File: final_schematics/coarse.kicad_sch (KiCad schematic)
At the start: 7 parts, among them J3 RJ9, SW1 SW_SPST, SW2 SW_SPST, SW3 SW_SPST, SW4 SW_SPST, SW5 SW_SPST

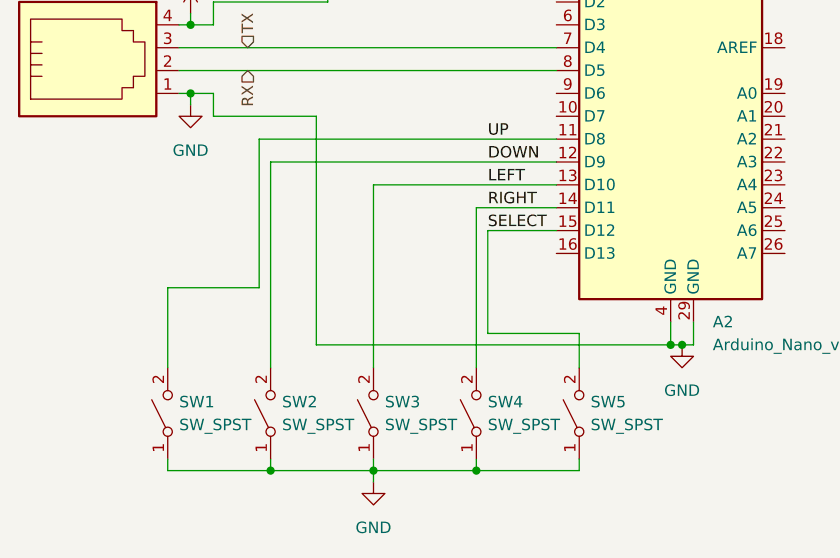
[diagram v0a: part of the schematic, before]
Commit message: Test code on main board
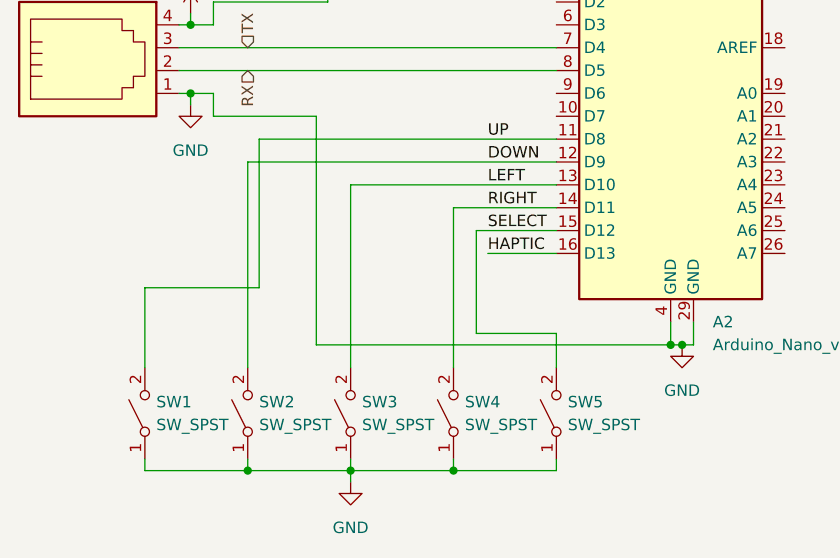
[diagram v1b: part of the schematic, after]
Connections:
- net HAPTIC: now reaches A2.16 (D13)
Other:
- moved on the sheet: SW1, SW2, SW3, SW4, SW5

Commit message: Almost ready to play a full game
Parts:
- added M2: Motor_DC, symbol Motor:Motor_DC
- added Q2: NPN, symbol Simulation_SPICE:NPN
- added R2: 330, symbol Device:R
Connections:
- net +5V: now also M2.1 (+)
- net GND: now also Q2.3 (E)
- net HAPTIC: now also R2.1
- new net: M2.2 (-), Q2.1 (C)
- new net: Q2.2 (B), R2.2

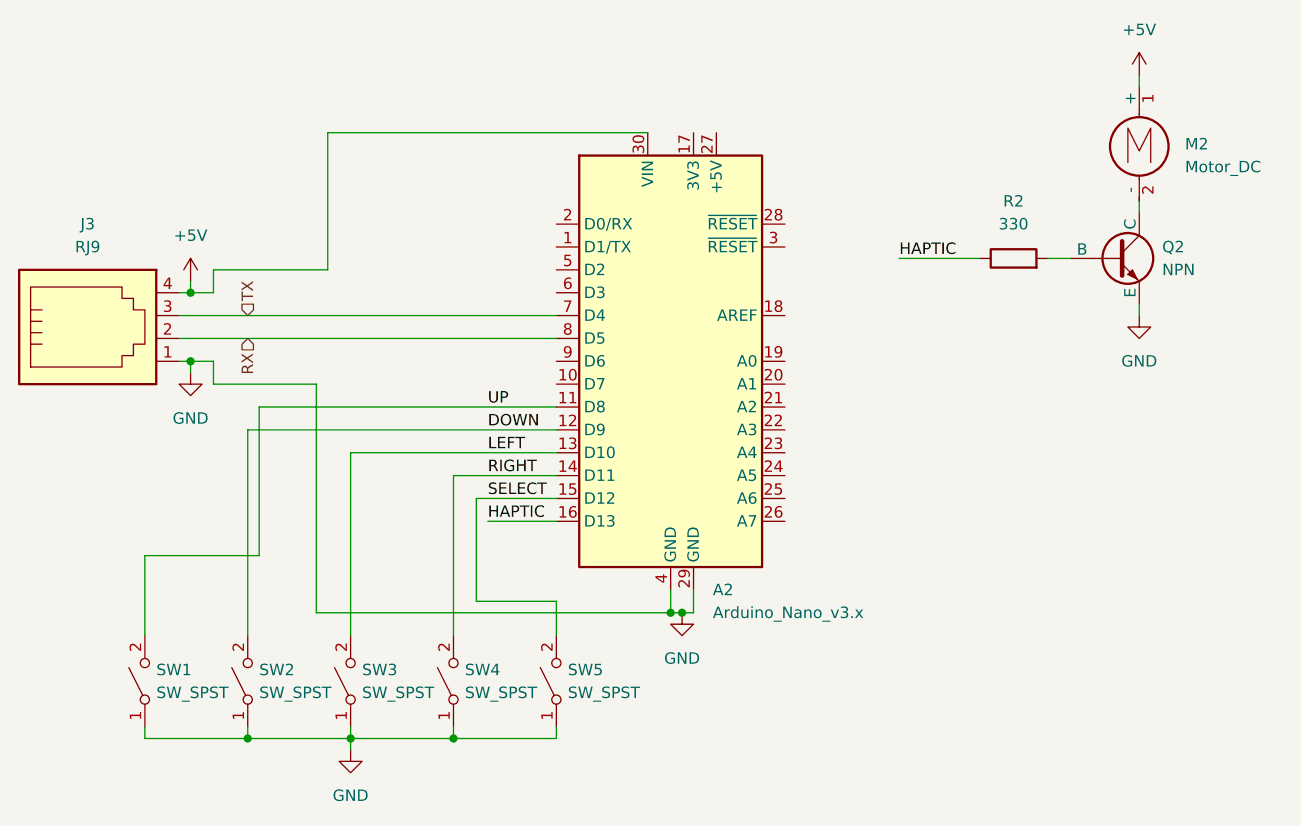
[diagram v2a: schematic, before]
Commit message: Add flowcharts
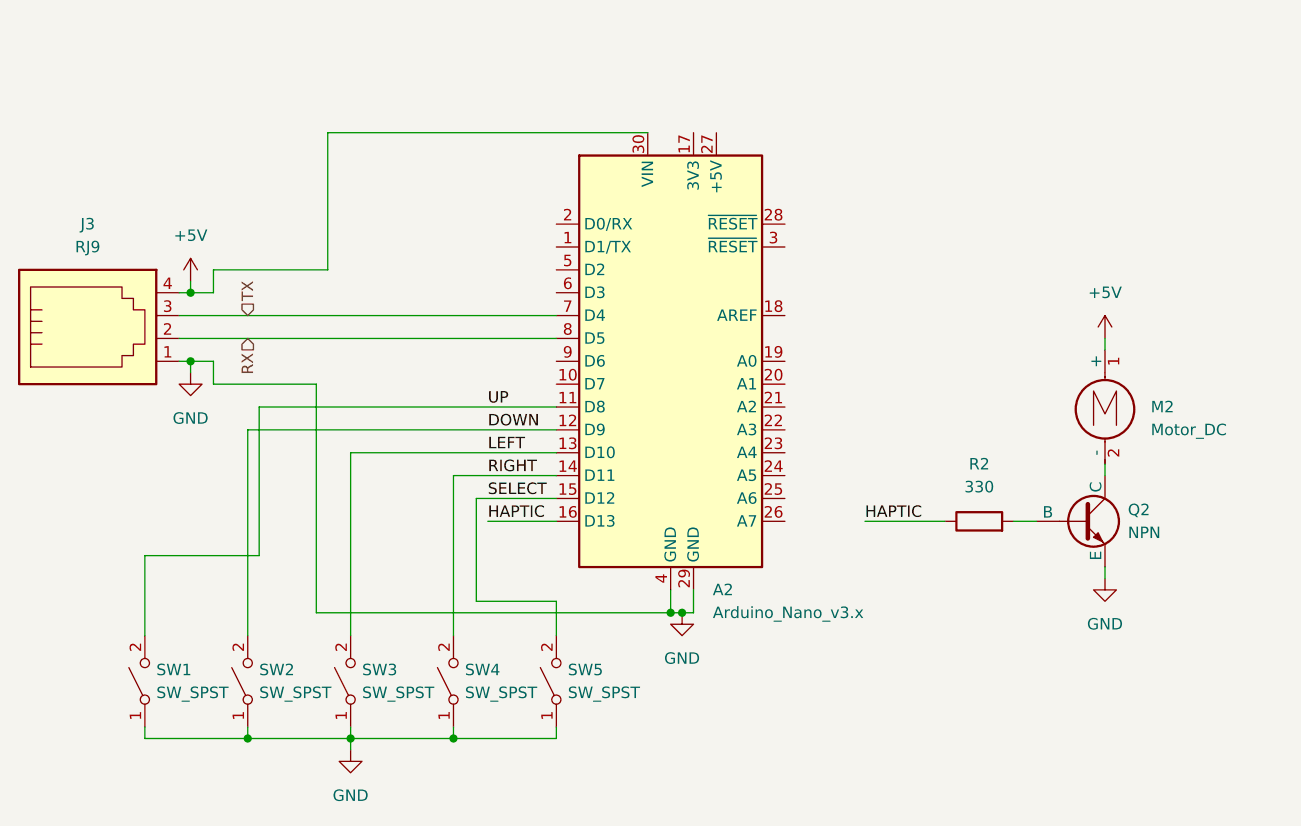
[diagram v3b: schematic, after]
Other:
- moved on the sheet: M2, Q2, R2
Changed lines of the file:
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@@
 	(wire
 		(pts
-			(xy 194.31 67.31) (xy 194.31 68.58)
+			(xy 190.5 96.52) (xy 190.5 97.79)
 		)
 		(stroke
@@
 	(wire
 		(pts
-			(xy 194.31 78.74) (xy 194.31 80.01)
-		)
-		(stroke
-			(width 0)
-			(type default)
-		)
-	)
-	(wire
-		(pts
-			(xy 167.64 73.66) (xy 176.53 73.66)
+			(xy 190.5 107.95) (xy 190.5 109.22)
+		)
+		(stroke
+			(width 0)
+			(type default)
+		)
+	)
+	(wire
+		(pts
+			(xy 163.83 102.87) (xy 172.72 102.87)
 		)
 		(stroke
@@
 	(wire
 		(pts
-			(xy 184.15 73.66) (xy 186.69 73.66)
+			(xy 180.34 102.87) (xy 182.88 102.87)
 		)
 		(stroke
@@
 	(wire
 		(pts
-			(xy 194.31 53.34) (xy 194.31 54.61)
+			(xy 190.5 82.55) (xy 190.5 83.82)
 		)
 		(stroke
@@
 	)
 	(label "HAPTIC"
-		(at 167.64 73.66 0)
+		(at 163.83 102.87 0)
 		(effects
 			(font
@@
 	(symbol
 		(lib_id "power:+5V")
-		(at 194.31 53.34 0)
+		(at 190.5 82.55 0)
 		(unit 1)
 		(exclude_from_sim no)
@@
 		(fields_autoplaced yes)
 		(property "Reference" "#PWR023"
-			(at 194.31 57.15 0)
+			(at 190.5 86.36 0)
 			(effects
 				(font
@@
 		)
 		(property "Value" "+5V"
-			(at 194.31 48.26 0)
+			(at 190.5 77.47 0)
 			(effects
 				(font
@@
 		)
 		(property "Footprint" ""
-			(at 194.31 53.34 0)
+			(at 190.5 82.55 0)
 			(effects
 				(font
@@
 		)
 		(property "Datasheet" ""
-			(at 194.31 53.34 0)
+			(at 190.5 82.55 0)
 			(effects
 				(font
@@
 		)
 		(property "Description" "Power symbol creates a global label with name \"+5V\""
-			(at 194.31 53.34 0)
+			(at 190.5 82.55 0)
 			(effects
 				(font
@@
 	(symbol
 		(lib_id "power:GND")
-		(at 194.31 80.01 0)
+		(at 190.5 109.22 0)
 		(unit 1)
 		(exclude_from_sim no)
@@
 		(fields_autoplaced yes)
 		(property "Reference" "#PWR022"
-			(at 194.31 86.36 0)
+			(at 190.5 115.57 0)
 			(effects
 				(font
@@
 		)
 		(property "Value" "GND"
-			(at 194.31 85.09 0)
+			(at 190.5 114.3 0)
 			(effects
 				(font
@@
 		)
 		(property "Footprint" ""
-			(at 194.31 80.01 0)
+			(at 190.5 109.22 0)
 			(effects
 				(font
@@
 		)
 		(property "Datasheet" ""
-			(at 194.31 80.01 0)
+			(at 190.5 109.22 0)
 			(effects
 				(font
@@
 		)
 		(property "Description" "Power symbol creates a global label with name \"GND\" , ground"
-			(at 194.31 80.01 0)
+			(at 190.5 109.22 0)
 			(effects
 				(font
@@
 	(symbol
 		(lib_id "Simulation_SPICE:NPN")
-		(at 191.77 73.66 0)
+		(at 187.96 102.87 0)
 		(unit 1)
 		(exclude_from_sim no)
@@
 		(fields_autoplaced yes)
 		(property "Reference" "Q2"
-			(at 196.85 72.3899 0)
+			(at 193.04 101.5999 0)
 			(effects
 				(font
@@
 		)
 		(property "Value" "NPN"
-			(at 196.85 74.9299 0)
+			(at 193.04 104.1399 0)
 			(effects
 				(font
@@
 		)
 		(property "Footprint" ""
-			(at 255.27 73.66 0)
+			(at 251.46 102.87 0)
 			(effects
 				(font
@@
 		)
 		(property "Datasheet" "https://ngspice.sourceforge.io/docs/ngspice-html-manual/manual.xhtml#cha_BJTs"
-			(at 255.27 73.66 0)
+			(at 251.46 102.87 0)
 			(effects
 				(font
@@
 		)
 		(property "Description" "Bipolar transistor symbol for simulation only, substrate tied to the emitter"
-			(at 191.77 73.66 0)
+			(at 187.96 102.87 0)
 			(effects
 				(font
@@
 		)
 		(property "Sim.Device" "NPN"
-			(at 191.77 73.66 0)
+			(at 187.96 102.87 0)
 			(effects
 				(font
@@
 		)
 		(property "Sim.Type" "GUMMELPOON"
-			(at 191.77 73.66 0)
+			(at 187.96 102.87 0)
 			(effects
 				(font
@@
 		)
 		(property "Sim.Pins" "1=C 2=B 3=E"
-			(at 191.77 73.66 0)
+			(at 187.96 102.87 0)
 			(effects
 				(font
@@
 	(symbol
 		(lib_id "Motor:Motor_DC")
-		(at 194.31 59.69 0)
+		(at 190.5 88.9 0)
 		(unit 1)
 		(exclude_from_sim no)
@@
 		(fields_autoplaced yes)
 		(property "Reference" "M2"
-			(at 199.39 60.9599 0)
+			(at 195.58 90.1699 0)
 			(effects
 				(font
@@
 		)
 		(property "Value" "Motor_DC"
-			(at 199.39 63.4999 0)
+			(at 195.58 92.7099 0)
 			(effects
 				(font
@@
 		)
 		(property "Footprint" ""
-			(at 194.31 61.976 0)
+			(at 190.5 91.186 0)
 			(effects
 				(font
@@
 		)
 		(property "Datasheet" "~"
-			(at 194.31 61.976 0)
+			(at 190.5 91.186 0)
 			(effects
 				(font
@@
 		)
 		(property "Description" "DC Motor"
-			(at 194.31 59.69 0)
+			(at 190.5 88.9 0)
 			(effects
 				(font
@@
 	(symbol
 		(lib_id "Device:R")
-		(at 180.34 73.66 90)
+		(at 176.53 102.87 90)
 		(unit 1)
 		(exclude_from_sim no)
@@
 		(fields_autoplaced yes)
 		(property "Reference" "R2"
-			(at 180.34 67.31 90)
+			(at 176.53 96.52 90)
 			(effects
 				(font
@@
 		)
 		(property "Value" "330"
-			(at 180.34 69.85 90)
+			(at 176.53 99.06 90)
 			(effects
 				(font
@@
 		)
 		(property "Footprint" ""
-			(at 180.34 75.438 90)
+			(at 176.53 104.648 90)
 			(effects
 				(font
@@
 		)
 		(property "Datasheet" "~"
-			(at 180.34 73.66 0)
+			(at 176.53 102.87 0)
 			(effects
 				(font
@@
 		)
 		(property "Description" "Resistor"
-			(at 180.34 73.66 0)
-			(effects
-				(font
+			(at 176.53 102.87 0)
+			(effects
+				(font
